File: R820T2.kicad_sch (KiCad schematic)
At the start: 28 parts, among them U7 R820T2

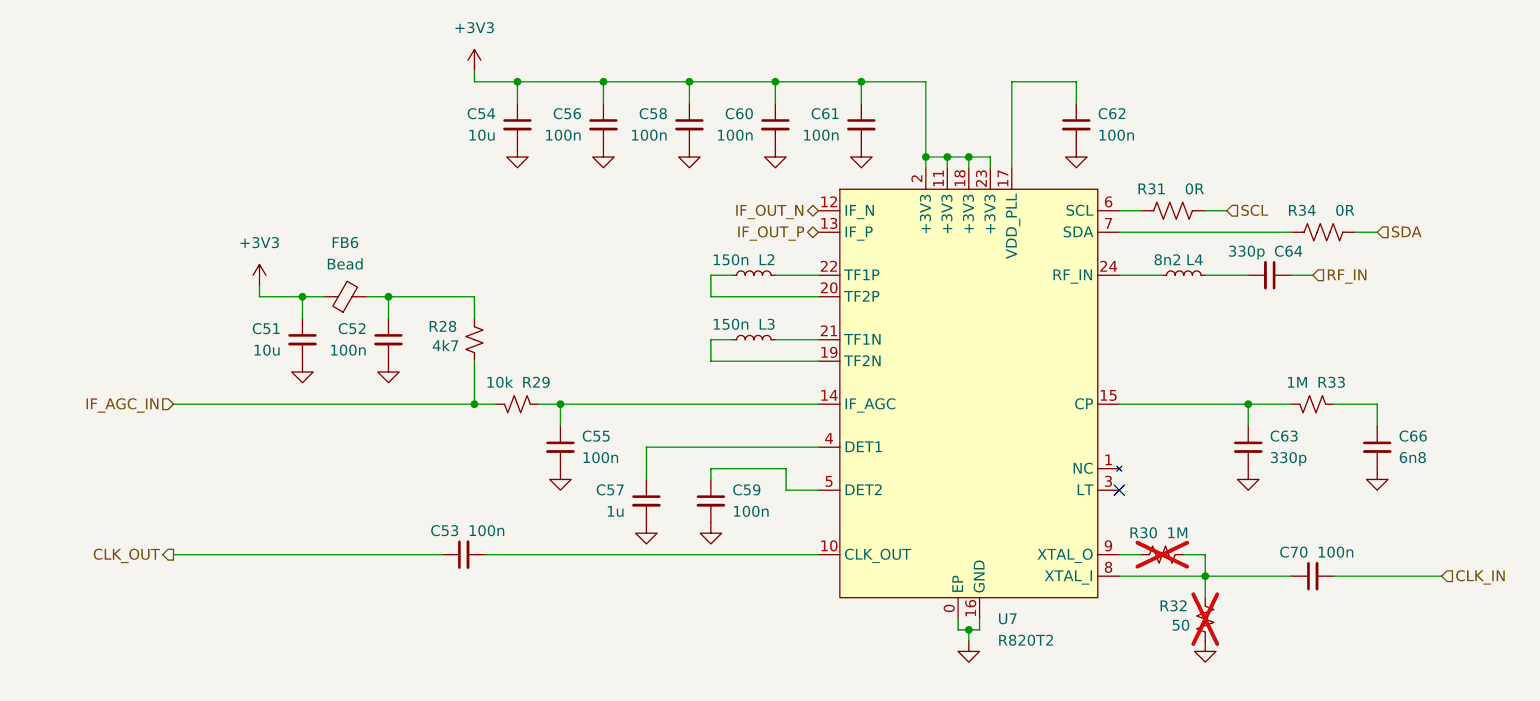
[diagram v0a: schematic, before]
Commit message: Schematic progress
I keep forgetting that I'm just making a panadapter here and not a full blown SDR...oops
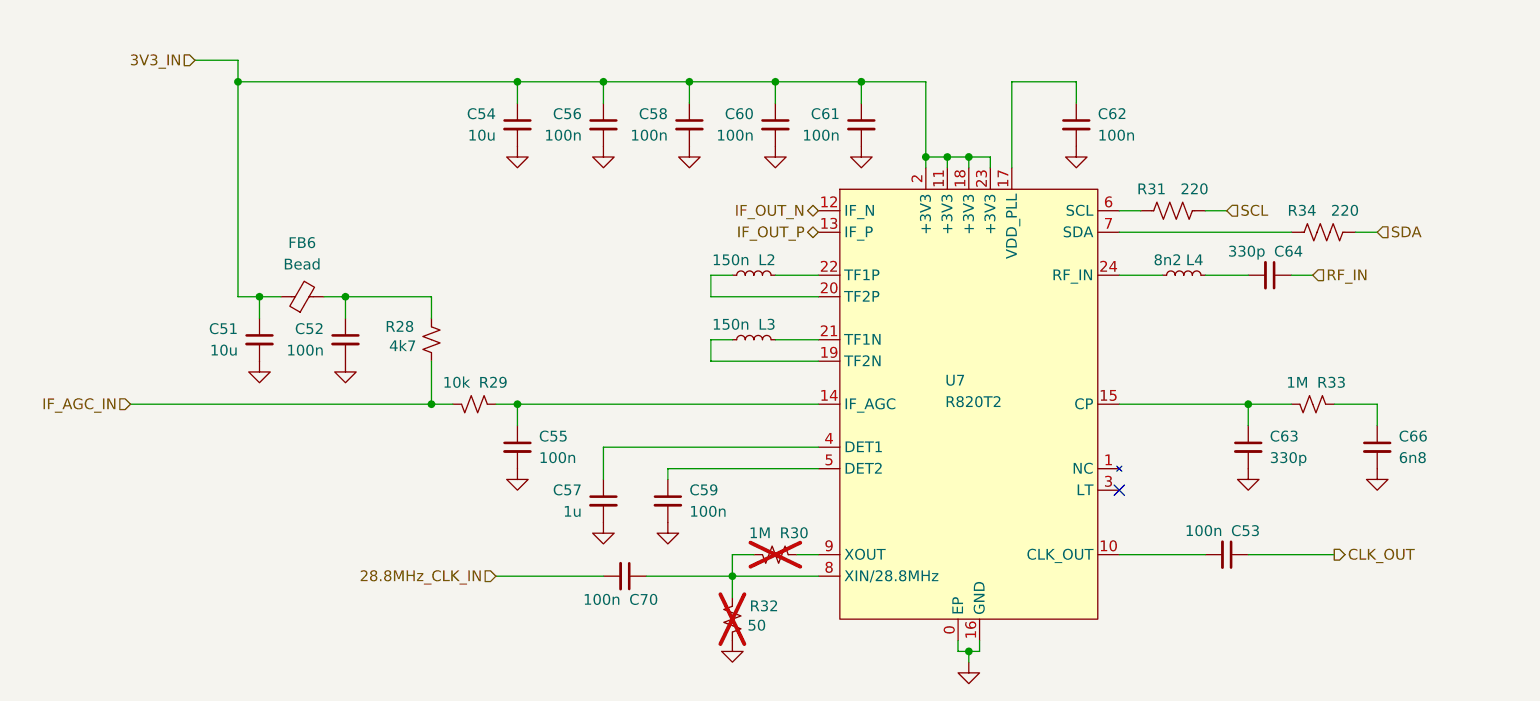
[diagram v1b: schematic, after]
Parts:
- R28, R29, R30, R33: footprint (none) -> libraries:Worthington_R_0402
- R31, R34: value 0R -> 220
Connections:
- net +3V3 renamed 3V3_IN
- net CLK_IN renamed 28.8MHz_CLK_IN
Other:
- moved on the sheet: C51, C52, C53, C55, C57, C59, C70, FB6, R28, R29, R30, R32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

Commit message: Schematic progress
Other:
- moved on the sheet: C51, C52, C53, C54, C55, C56, C57, C58, C59, C60, C61, C62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

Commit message: Schematic progress
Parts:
- removed C53: 100n, libraries:Worthington_C_0402, symbol Device:C_Small
- removed C54: 10u, libraries:Worthington_C_0603, symbol Device:C_Small
- removed R32: 50, Resistor_SMD:R_0805_2012Metric, symbol Device:R_Small_US
- added C96, C97: 100n, libraries:Worthington_C_0201, symbol Device:C_Small
- C51: footprint libraries:Worthington_C_0603 -> libraries:Worthington_C_0402; DigiKey (none) -> 4713-GMC04X5R106M10NTCT-ND; Manufacturer Part Number (none) -> GMC04X5R106M10NT; Voltage (none) -> 10V
- C52: value 100n -> 10u; DigiKey (none) -> 4713-GMC04X5R106M10NTCT-ND; Manufacturer Part Number (none) -> GMC04X5R106M10NT; Voltage (none) -> 10V
- C55, C56, C58, C59, C60, C61, C62, C70: footprint libraries:Worthington_C_0402 -> libraries:Worthington_C_0201; DigiKey (none) -> 445-15903-1-ND; Manufacturer Part Number (none) -> C0603X6S1C104K030BC; Voltage (none) -> 16V
- C57: footprint libraries:Worthington_C_0402 -> libraries:Worthington_C_0201; DigiKey (none) -> 4713-GMC02X5R105K10NTCT-ND; Manufacturer Part Number (none) -> GMC02X5R105K10NT; Voltage (none) -> 10V
- C63, C64: footprint libraries:Worthington_C_0402 -> libraries:Worthington_C_0201; DigiKey (none) -> 4713-GMC02X7R331J50NTCT-ND; Manufacturer Part Number (none) -> GMC02X7R331J50NT; Voltage (none) -> 50V
- C66: footprint libraries:Worthington_C_0402 -> libraries:Worthington_C_0201; DigiKey (none) -> 4713-GMC02X5R682K25NTCT-ND; Manufacturer Part Number (none) -> GMC02X5R682K25NT; Voltage (none) -> 25V
- FB6: footprint (none) -> libraries:Worthington_L_0402; now not fitted
- L2, L3: footprint (none) -> libraries:Worthington_L_0603; DigiKey (none) -> 490-6924-1-ND; Manufacturer Part Number (none) -> LQW18ANR15J00D
- L4: value 8n2 -> 8n2, ±2%; footprint (none) -> libraries:Worthington_L_0603; DigiKey (none) -> 490-LQW18AS8N2G00DCT-ND; Manufacturer Part Number (none) -> LQW18AS8N2G00D
- R28, R29, R30, R33: footprint libraries:Worthington_R_0402 -> libraries:Worthington_R_0201
- R31, R34: footprint Resistor_SMD:R_0603_1608Metric_Pad0.98x0.95mm_HandSolder -> libraries:Worthington_R_0201
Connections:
- net 28.8MHz_CLK_IN: now also C96.1; no longer C70.2
- net 3V3_IN: now also C52.1
- net CLK_OUT: now also C97.2
- net GND: now also C70.2
- net SCL: now also R31.1; no longer R31.2
- net SDA: now also R34.1; no longer R34.2
- net at U7.7 (SDA): now also R34.2; no longer R34.1
- net at R30.2, U7.8 (XIN/28.8MHz): now also C96.2; no longer C70.1
- net at U7.10 (CLK_OUT): now also C97.1
- net at U7.6 (SCL): now also R31.2; no longer R31.1
- net at FB6.2, R28.2: now also C70.1; no longer C52.1
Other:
- moved on the sheet: C66, L2, L4, R31, R33, R34

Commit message: Schematic and PCB progress
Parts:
- renumbered C66 to C50, C64 to C51, C96 to C52, C63 to C53, C62 to C54, C56 to C55, C58 to C56, C97 to C57, C60 to C58, C61 to C60, C57 to C61, C52 to C62, C55 to C63, C70 to C64, C51 to C65, L4 to L2, L2 to L3, L3 to L4, R33 to R44, R31 to R45, R34 to R46, R30 to R47, R29 to R48, R28 to R49, U7 to U9
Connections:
- net GND: now also U9.25 (EP); no longer U9.0 (EP)

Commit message: PCB Layout Progress
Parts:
- removed FB6: Bead, libraries:Worthington_L_0402, symbol Device:FerriteBead_Small
- L2, L3, L4: footprint libraries:Worthington_L_0603 -> libraries:Worthington_L_0603_RF
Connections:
- net 3V3_IN: now also C64.1, R49.2
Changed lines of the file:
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@@
 	)
 	(junction
-		(at 203.2 110.49)
+		(at 281.94 127)
 		(diameter 0)
 		(color 0 0 0 0)
 	)
 	(junction
-		(at 220.98 101.6)
+		(at 203.2 110.49)
 		(diameter 0)
 		(color 0 0 0 0)
 	)
 	(junction
-		(at 200.66 110.49)
+		(at 220.98 101.6)
 		(diameter 0)
 		(color 0 0 0 0)
 	)
 	(junction
-		(at 165.1 139.7)
+		(at 200.66 110.49)
 		(diameter 0)
 		(color 0 0 0 0)
 	)
 	(junction
-		(at 281.94 127)
+		(at 165.1 139.7)
 		(diameter 0)
 		(color 0 0 0 0)
 	)
 	(junction
-		(at 271.78 127)
+		(at 198.12 168.91)
 		(diameter 0)
 		(color 0 0 0 0)
 	)
 	(junction
-		(at 198.12 168.91)
+		(at 210.82 101.6)
 		(diameter 0)
 		(color 0 0 0 0)
 	)
 	(junction
-		(at 210.82 101.6)
+		(at 261.62 139.7)
 		(diameter 0)
 		(color 0 0 0 0)
 	)
 	(junction
-		(at 261.62 139.7)
+		(at 271.78 127)
 		(diameter 0)
 		(color 0 0 0 0)
@@
 	(wire
 		(pts
-			(xy 271.78 127) (xy 274.32 127)
+			(xy 271.78 127) (xy 281.94 127)
 		)
 		(stroke
@@
 	(wire
 		(pts
-			(xy 279.4 127) (xy 281.94 127)
-		)
-		(stroke
-			(width 0)
-			(type default)
-		)
-	)
-	(wire
-		(pts
 			(xy 193.04 101.6) (xy 193.04 111.76)
 		)
@@
 			)
 		)
-		(property "Footprint" "libraries:Worthington_L_0603"
+		(property "Footprint" "libraries:Worthington_L_0603_RF"
 			(at 226.06 124.46 0)
 			(hide yes)
@@
 			)
 		)
-		(property "Footprint" "libraries:Worthington_L_0603"
+		(property "Footprint" "libraries:Worthington_L_0603_RF"
 			(at 161.29 132.08 0)
 			(hide yes)
@@
 	)
 	(symbol
-		(lib_id "Device:FerriteBead_Small")
-		(at 276.86 127 270)
-		(mirror x)
-		(unit 1)
-		(body_style 1)
-		(exclude_from_sim no)
-		(in_bom yes)
-		(on_board yes)
-		(in_pos_files yes)
-		(dnp yes)
-		(fields_autoplaced yes)
-		(property "Reference" "FB6"
-			(at 276.8981 120.65 90)
-			(show_name no)
-			(do_not_autoplace no)
-			(effects
-				(font
-					(size 1.27 1.27)
-				)
-			)
-		)
-		(property "Value" "Bead"
-			(at 276.8981 123.19 90)
-			(show_name no)
-			(do_not_autoplace no)
-			(effects
-				(font
-					(size 1.27 1.27)
-				)
-			)
-		)
-		(property "Footprint" "libraries:Worthington_L_0402"
-			(at 276.86 128.778 90)
-			(hide yes)
-			(show_name no)
-			(do_not_autoplace no)
-			(effects
-				(font
-					(size 1.27 1.27)
-				)
-			)
-		)
-		(property "Datasheet" ""
-			(at 276.86 127 0)
-			(hide yes)
-			(show_name no)
-			(do_not_autoplace no)
-			(effects
-				(font
-					(size 1.27 1.27)
-				)
-			)
-		)
-		(property "Description" "Ferrite bead, small symbol"
-			(at 276.86 127 0)
-			(hide yes)
-			(show_name no)
-			(do_not_autoplace no)
-			(effects
-				(font
-					(size 1.27 1.27)
-				)
-			)
-		)
-		(pin "1"
-		)
-		(pin "2"
-		)
-		(instances
-			(project "PiZero_RTL_Panadapter"
-				(path "/9dbbaad8-804a-4efe-a989-bc17c5acbd91/cec674a5-f6d8-4c83-b8c1-07bf170daffc"
-					(reference "FB6")
-					(unit 1)
-				)
-			)
-		)
-	)
-	(symbol
 		(lib_id "power:GND")
 		(at 231.14 109.22 0)
@@
 			)
 		)
-		(property "Footprint" "libraries:Worthington_L_0603"
+		(property "Footprint" "libraries:Worthington_L_0603_RF"
 			(at 226.06 132.08 0)
 			(hide yes)

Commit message: PCB and schematic progress
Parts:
- removed C65: 10u, libraries:Worthington_C_0402, symbol Device:C_Small
- removed R45, R46: 220, libraries:Worthington_R_0201, symbol Device:R_US
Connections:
- net SCL: now also U9.6 (SCL)
- net SDA: now also U9.7 (SDA)
